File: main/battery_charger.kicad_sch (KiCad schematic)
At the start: 31 parts, among them Q601 IXTP28P065T, Q602 TK4R3E06PL, U601 LT8710

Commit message: Some work
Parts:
- removed C601, C602: 10u, symbol Device:C
- removed C603: 100u, symbol Device:C_Polarized
- removed C604: 4x10u, symbol Device:C
- removed C605, C609: C, symbol Device:C
- removed C606: 200u, symbol Device:C_Polarized
- removed C607, C608: 2.2u, symbol Device:C
- removed C610: 62n, symbol Device:C
- removed C611: 100p, symbol Device:C
- removed C612: 560n, symbol Device:C
- removed C613: 4.7n, symbol Device:C
- removed JP601, JP602: JP_COMP, symbol Jumper:SolderJumper_2_Bridged
- removed L601: 3.3u, symbol Device:L_Coupled_1324
- removed Q601: IXTP28P065T, symbol Device:Q_PMOS_GDS
- removed Q602: TK4R3E06PL, Package_TO_SOT_THT:TO-220-3_Horizontal_TabUp, symbol Device:Q_NMOS_GDS
- removed R601: 33m, symbol Device:R
- removed R602: 1m, symbol Device:R
- removed R603: 18k, symbol Device:R
- removed R604: 4.7k, symbol Device:R
- removed R605: 200k, symbol Device:R
- removed R606, R608: R, symbol Device:R
- removed R607: 120k, symbol Device:R
- removed R609: 22k, symbol Device:R
- removed RV601: 100k (10k), symbol Device:R_Potentiometer
- removed TP601: TP_RCOMP_H, symbol Connector:TestPoint
- removed TP602: TP_RCOMP_L, symbol Connector:TestPoint
- removed U601: LT8710, Package_SO:HTSSOP-20-1EP_4.4x6.5mm_P0.65mm_EP2.74x3.86mm, symbol power_supply:LT8710
- added C1601, C1602: 10u, symbol Device:C
- added C1603: 100u, symbol Device:C_Polarized
- added C1604: 4x10u, symbol Device:C
- added C1605: C, symbol Device:C
- added C1606: 200u, symbol Device:C_Polarized
- added C1607, C1608: 2.2u, symbol Device:C
- added C1610: 62n, symbol Device:C
- added C1611: 100p, symbol Device:C
- added C1612: 560n, symbol Device:C
- added C1613: 4.7n, symbol Device:C
- added D1601, D1602: D, symbol Device:D
- added JP1601, JP1602: JP_COMP, symbol Jumper:SolderJumper_2_Bridged
- added L1601: 3.3u, symbol Device:L_Coupled_1324
- added Q1601, Q1602: Q_PMOS_DGS, symbol Device:Q_PMOS_DGS
- added Q1603: Q_NMOS_DGS, symbol Device:Q_NMOS_DGS
- added Q1604: IXTP28P065T, symbol Device:Q_PMOS_GDS
- added Q1605: TK4R3E06PL, Package_TO_SOT_THT:TO-220-3_Horizontal_TabUp, symbol Device:Q_NMOS_GDS
- added R1601, R1602: 10k, symbol Device:R
- added R1603: 33m, symbol Device:R
- added R1604: 1m, symbol Device:R
- added R1605: 18k, symbol Device:R
- added R1606: 4.7k, symbol Device:R
- added R1607: 200k, symbol Device:R
- added R1609: 120k, symbol Device:R
- added R1610: R, symbol Device:R
- added R1611: 22k, symbol Device:R
- added RV1601: 100k (10k), symbol Device:R_Potentiometer
- added TP1601: TP_RCOMP_H, symbol Connector:TestPoint
- added TP1602: TP_RCOMP_L, symbol Connector:TestPoint
- added U1601: LT8710, Package_SO:HTSSOP-20-1EP_4.4x6.5mm_P0.65mm_EP2.74x3.86mm, symbol power_supply:LT8710
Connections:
- net PGND: now also C1603.2, C1604.2, C1605.2, C1606.2, C1608.2, C1610.2, C1611.2, C1612.2, C1613.2, L1601.2, R1604.2, R1606.2, R1611.2, U1601.14 (CSN), U1601.19 (SYNC), U1601.20 (GND), U1601.21 (PAD)
- net V_{IN}: now also C1603.1, C1604.1, L1601.1, R1605.1, U1601.13 (V_{IN})
- net V_{OUT}: now also C1605.1, C1606.1, C1607.1, R1603.2, R1607.1, U1601.6 (ISN), U1601.8 (BIAS)
- new net: JP1601.2 (B), RV1601.1, RV1601.2, TP1601.1
- new net: C1612.1, U1601.3 (SS)
- new net: Q1601.1 (D), Q1602.1 (D)
- new net: D1601.2 (A), Q1601.2 (G), R1601.2
- new net: Q1605.1 (G), U1601.11 (BG)
- new net: C1601.2, C1602.2, L1601.3, Q1605.2 (D)
- new net: Q1605.3 (S), R1604.1, U1601.15 (CSP)
- new net: C1601.1, C1602.1, L1601.4, Q1604.2 (D)
- new net: C1607.2, U1601.9 (INTV_{EE})
- new net: C1611.1, JP1601.1 (A), R1610.1, U1601.2 (V_{c})
- new net: C1613.1, JP1602.1 (A), R1610.2
- new net: R1607.2, U1601.1 (FBX)
- new net: Q1604.1 (G), U1601.10 (TG)
- new net: C1608.1, U1601.12 (INTV_{CC}), U1601.17 (MODE)
- new net: R1605.2, R1606.1, U1601.16 (EN/FBIN)
- new net: R1609.1, U1601.18 (RT)
- new net: C1610.1, U1601.5 (IMON)
- new net: Q1604.3 (S), R1603.1, U1601.7 (ISP)
- new net: JP1602.2 (B), RV1601.3, TP1602.1
- new net: R1609.2, R1611.1
- new net: D1602.2 (A), Q1602.2 (G), R1602.2
- new net: D1601.1 (K), D1602.1 (K), Q1603.1 (D)
- new net EN: Q1603.2 (G)
- new net GND: Q1603.3 (S)
- new net VBATT: Q1602.3 (S), R1602.1
- new net VCAP: Q1601.3 (S), R1601.1
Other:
- note added: "Target output is 12.4V Nominal, 2.2A @ 12.4V"
- note removed: "If required, solder R and C for external V_{OUT} control. Note that the external control can only *lower* the output voltage."
- note removed: "Target output is 18V Therefore, at most, 2.2A @ 18V Using max cell current when caps discharged (5A) We should handle 37.5W/5A/18V (not all same time)"
- company: Julien FAUCHER -> (none)
- title: MPPT PSU - Core boost converter -> (none)

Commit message: Update
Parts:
- removed Q1601, Q1602: Q_PMOS_DGS, symbol Device:Q_PMOS_DGS
- added Q1601, Q1608: IXTP28P065T, symbol Device:Q_PMOS_GDS
- added Q1606, Q1607: Q_NMOS_GDS, symbol Device:Q_NMOS_GDS
- added R1608, R1613: 4.7k, symbol Device:R
- added R1612, R1614: 10k, symbol Device:R
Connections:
- net GND is gone; now on net PGND: Q1603.3 (S)
- net PGND: now also Q1606.3 (S), Q1607.3 (S), R1612.2, R1614.2
- net at D1601.2 (A), R1601.2: now also Q1601.1 (G)
- net at R1605.2, R1606.1, U1601.16 (EN/FBIN): now also Q1606.2 (D), Q1607.2 (D)
- net at D1602.2 (A), R1602.2: now also Q1608.1 (G)
- net EN renamed BAT_USE
- net BAT_USE: now also R1613.1, R1614.1
- net VBATT renamed RETURN_PATH_2
- net RETURN_PATH_2: now also Q1608.3 (S)
- net VCAP renamed RETURN_PATH_1
- net RETURN_PATH_1: now also Q1601.3 (S)
- new net: Q1607.1 (G), R1613.2
- new net: Q1606.1 (G), R1608.2
- new net: Q1601.2 (D), Q1608.2 (D)
- new net ~{BAT_CHRG}: R1608.1, R1612.1
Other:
- note added: "Coeff of 0.207 for start of regulation on MPP and avoiding input supply collapse under 8V End of regu on -6%"
- note added: "Input from 2*8*35F at up to 18V"
- note removed: "Coeff of 0.207 for start of regulation on MPP End of regu on -7.5%"
- note removed: "Input from 14 SunPower C60 (0.22m^{2}) - 0.6V MPP 0.7V OC - 5.7A MPP 6.0A CC Given 80% sunlight from France: Nominal 8.0V @ 4.7A (37.5W)"
- moved on the sheet: D1601, D1602, Q1603, R1601, R1602, R1606

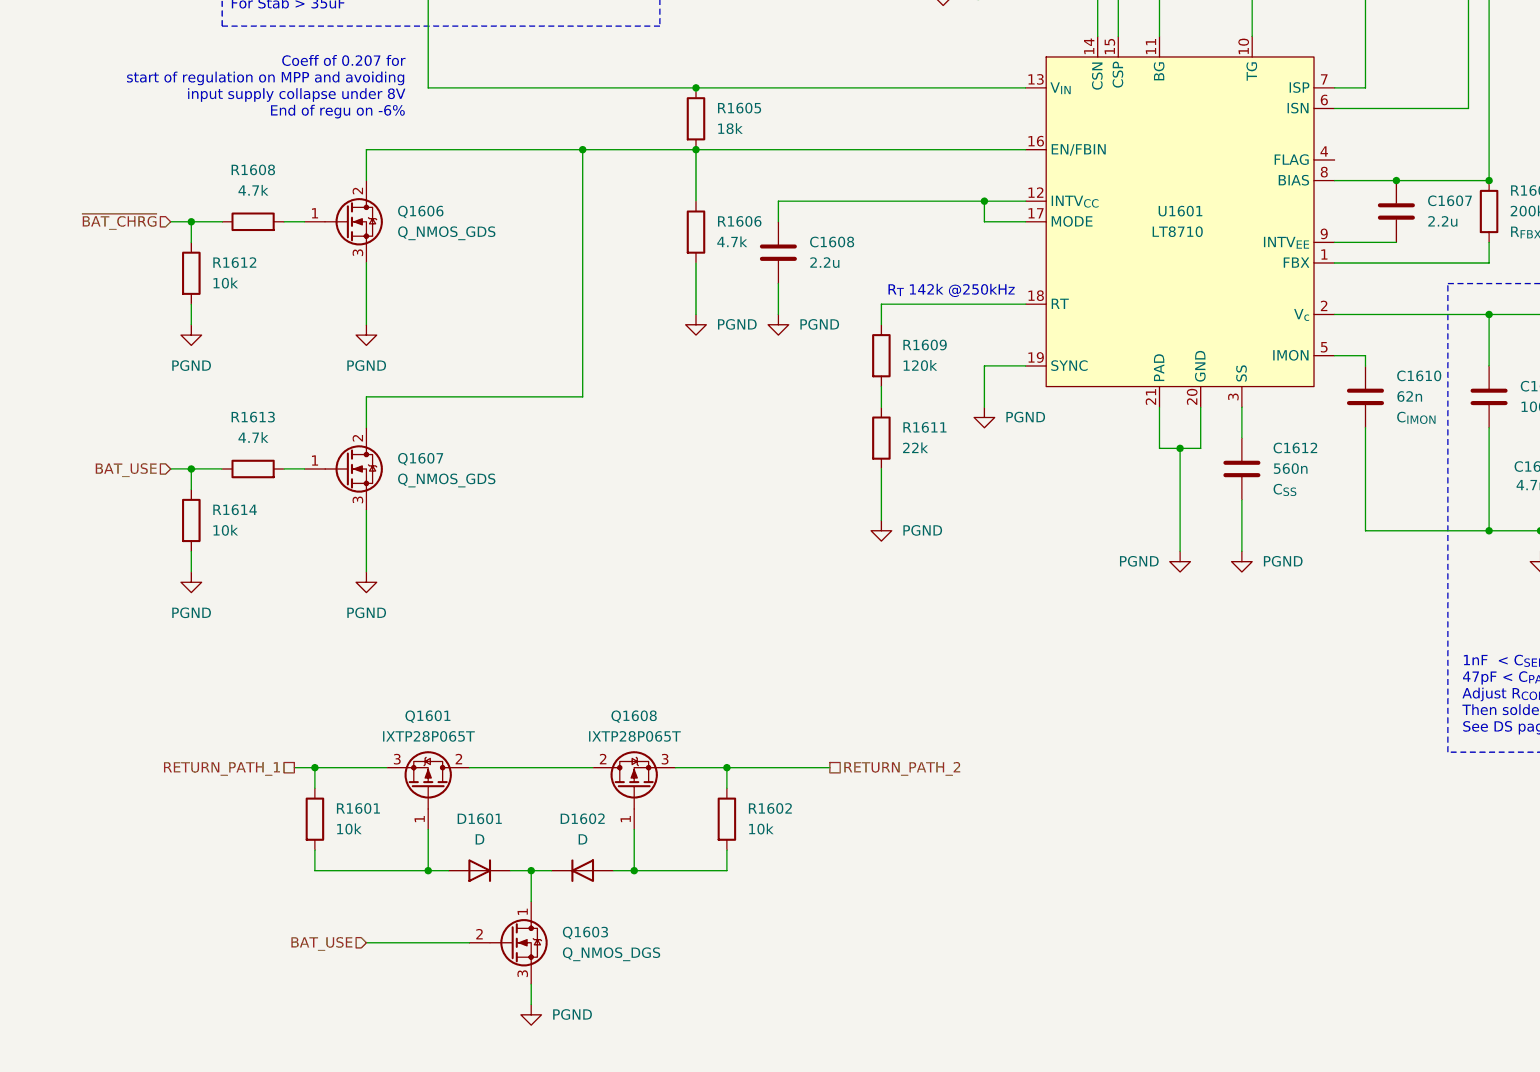
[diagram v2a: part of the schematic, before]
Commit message: Finalize schema for bat charger
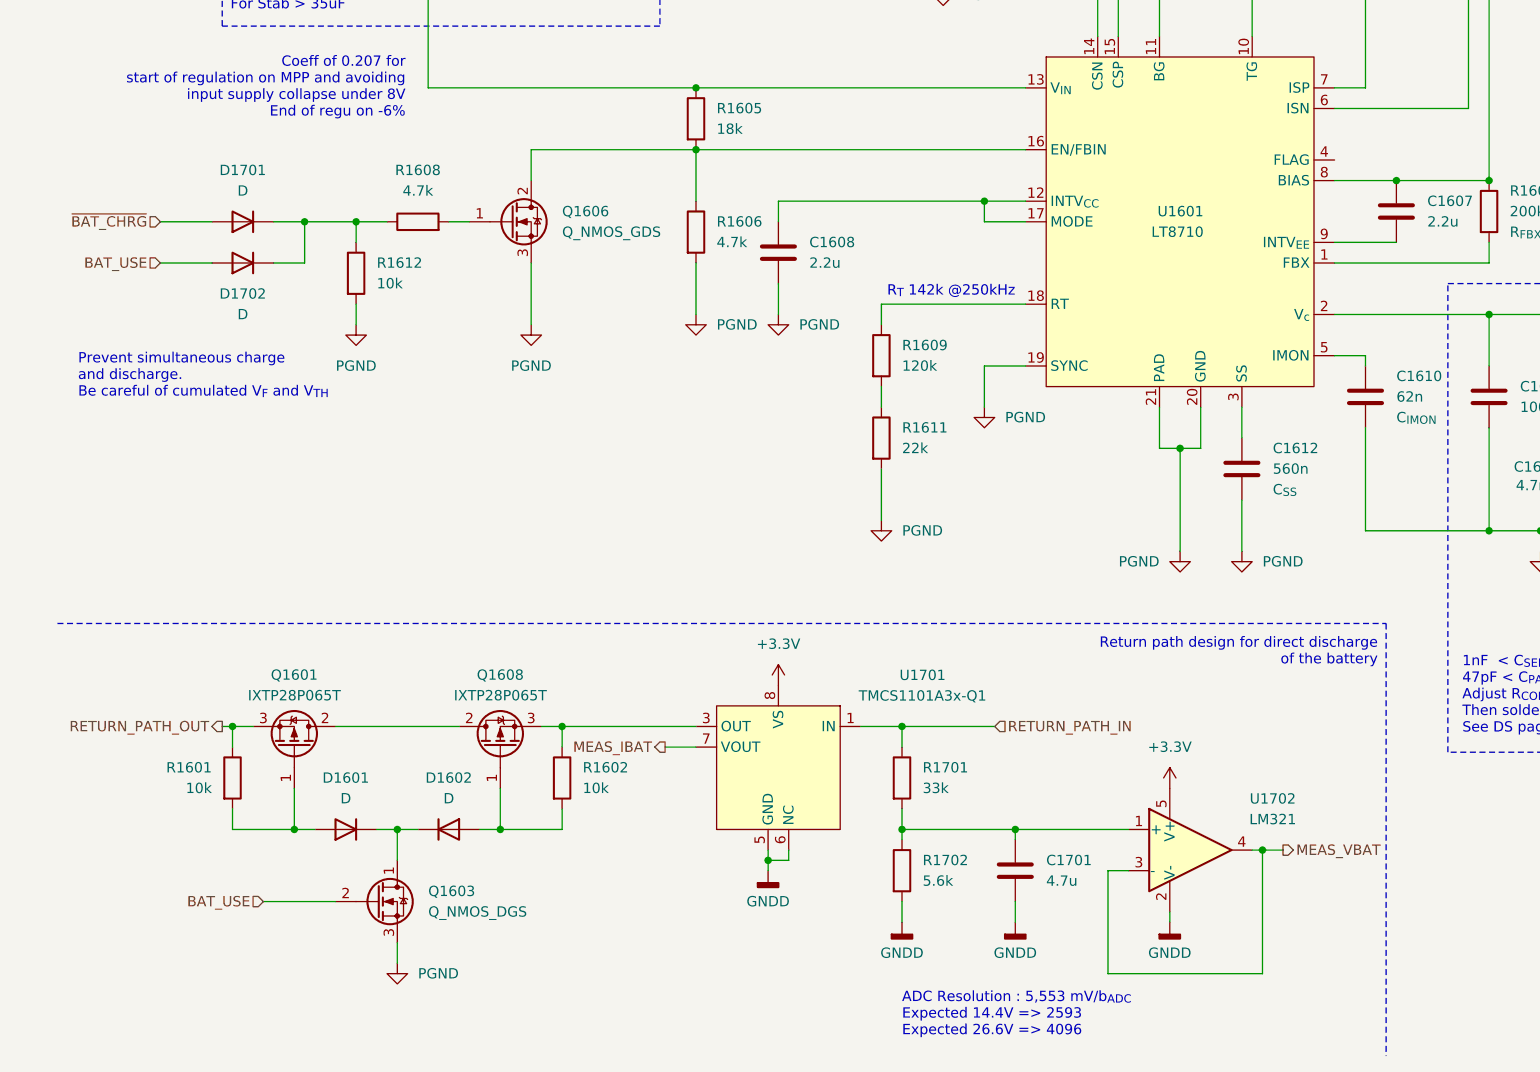
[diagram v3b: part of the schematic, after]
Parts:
- removed Q1607: Q_NMOS_GDS, symbol Device:Q_NMOS_GDS
- removed R1613: 4.7k, symbol Device:R
- removed R1614: 10k, symbol Device:R
- added C1701: 4.7u, symbol Device:C
- added D1701, D1702: D, symbol Device:D
- added R1701: 33k, symbol Device:R
- added R1702: 5.6k, symbol Device:R
- added U1701: TMCS1101A3x-Q1, symbol dsv4:TMCS1101
- added U1702: LM321, Package_TO_SOT_SMD:SOT-23-5, symbol Amplifier_Operational:LM321
- R1602: now left out of the parts list
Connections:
- net BAT_USE: now also D1702.2 (A)
- net ~{BAT_CHRG}: now also D1701.2 (A); no longer R1608.1, R1612.1
- net RETURN_PATH_1 renamed RETURN_PATH_OUT
- net RETURN_PATH_2: no longer names the net of Q1608.3 (S), R1602.1
- net RETURN_PATH_2: now also U1701.3 (OUT), U1701.4 (OUT)
- new net: C1701.1, R1701.2, R1702.1, U1702.1 (+)
- new net: D1701.1 (K), D1702.1 (K), R1608.1, R1612.1
- new net +3.3V: U1701.8 (VS), U1702.5 (V+)
- new net GNDD: C1701.2, R1702.2, U1701.5 (GND), U1701.6 (NC), U1702.2 (V-)
- new net IN: R1701.1, U1701.1 (IN), U1701.2 (IN)
- new net MEAS_IBAT: U1701.7 (VOUT)
- new net MEAS_VBAT: U1702.3 (-), U1702.4
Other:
- note added: "ADC Resolution : 5,553 mV/b_{ADC} Expected 14.4V => 2593 Expected 26.6V => 4096"
- note added: "Prevent simultaneous charge and discharge. Be careful of cumulated V_{F} and V_{TH}"
- note added: "Return path design for direct discharge of the battery"
- moved on the sheet: D1601, D1602, Q1601, Q1603, Q1606, Q1608, R1601, R1602, R1608, R1612
